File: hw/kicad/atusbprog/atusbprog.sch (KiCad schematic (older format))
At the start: 26 parts, among them J1 SMH-110-02-L-D, J2 Conn_01x04, J3 Conn_01x08, J4 Conn_01x08, J5 Conn_01x08, SW1 SW_Push, SW2 SW_Push, U1 SN74HCT125, U2 AT89S52-24PU, Y1 24 MHz

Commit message: Update to KiCAD 5.1.5, add silk marks
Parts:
- RN1: footprint Resistor_THT:R_Array_SIP9 -> Resistors_THT:R_Array_SIP9
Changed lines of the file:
@@
 EESchema Schematic File Version 4
-LIBS:atusbprog-cache
-EELAYER 26 0
+EELAYER 30 0
 EELAYER END
 $Descr A4 11693 8268
@@
 F 0 "RN1" H 10180 2196 50  0000 L CNN
 F 1 "1.2k" H 10180 2105 50  0000 L CNN
-F 2 "Resistor_THT:R_Array_SIP9" V 10275 2150 50  0001 C CNN
+F 2 "Resistors_THT:R_Array_SIP9" V 10275 2150 50  0001 C CNN
 F 3 "https://www.bourns.com/docs/Product-Datasheets/4600x.pdf" H 9800 2150 50  0001 C CNN
 	1    9800 2150

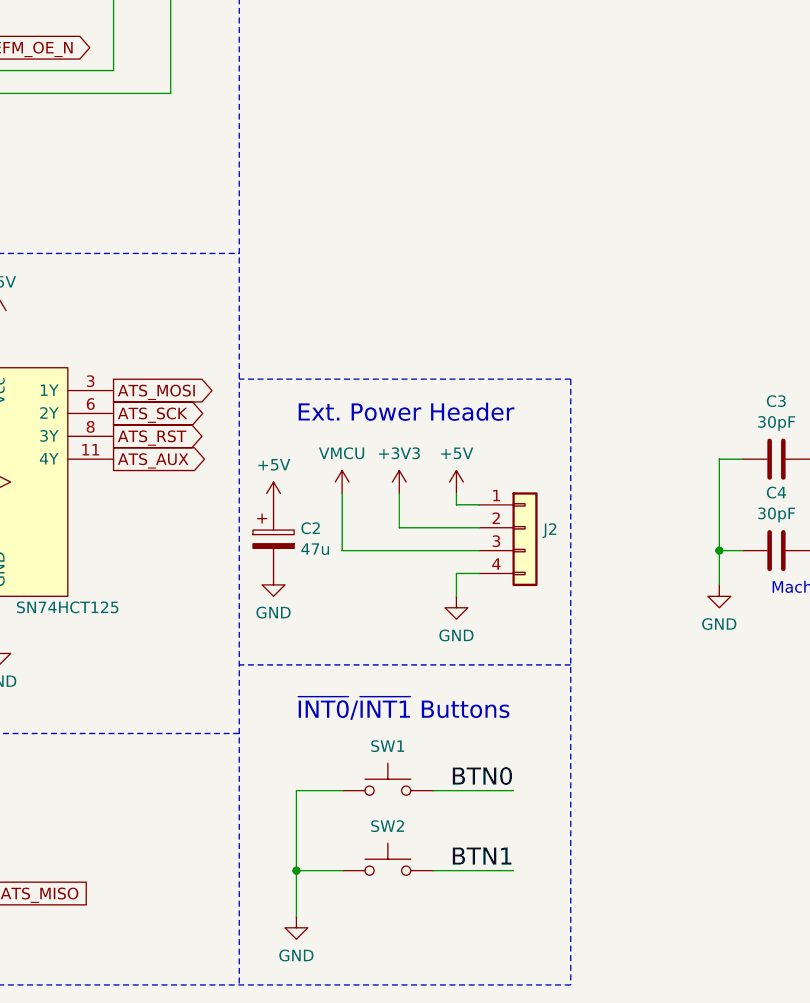
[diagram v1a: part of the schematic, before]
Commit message: Add power LEDs
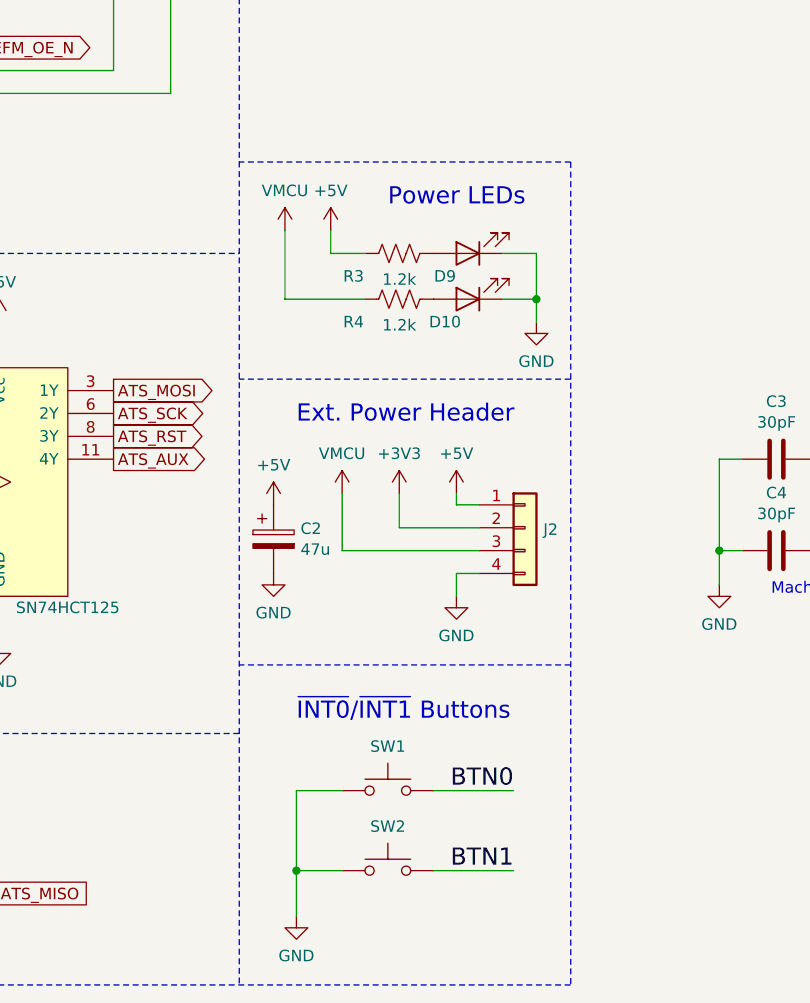
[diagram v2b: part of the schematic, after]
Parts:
- added D10: LTL2R3KYD-EM, LEDs:LED_D5.0mm, symbol Device:LED
- added D9: LTL2R3KRD-EM, LEDs:LED_D5.0mm, symbol Device:LED
- added R3, R4: 1.2k, Resistors_THT:R_Axial_DIN0207_L6.3mm_D2.5mm_P7.62mm_Horizontal, symbol Device:R_US
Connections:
- net +5V: now also R3.1
- net +VMCU: now also R4.1
- net GND: now also D10.1 (K), D9.1 (K)
- new net: D10.2 (A), R4.2
- new net: D9.2 (A), R3.2
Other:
- note added: "Power LEDs"
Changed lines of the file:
@@
 Ext. Power Header
-Wire Notes Line
-	4800 4350 4800 7000
 Wire Notes Line
 	4800 5600 3350 5600
 Wire Notes Line
 	4800 4350 3350 4350
+$Comp
+L Device:LED D10
+U 1 1 5E8A95B0
+P 4350 4000
+F 0 "D10" H 4450 4100 50  0000 C CNN
+F 1 "LTL2R3KYD-EM" V 4297 3883 50  0001 R CNN
+F 2 "LEDs:LED_D5.0mm" H 4350 4000 50  0001 C CNN
+F 3 "https://media.digikey.com/pdf/Data%20Sheets/Lite-On%20PDFs/LTL2R3KGD-EM%20Preliminary.pdf" H 4350 4000 50  0001 C CNN
+	1    4350 4000
+	-1   0    0    1
+$EndComp
+$Comp
+L Device:R_US R4
+U 1 1 5E8AEB1D
+P 4050 4000
+F 0 "R4" V 3950 4200 50  0000 C CNN
+F 1 "1.2k" V 3936 4000 50  0000 C CNN
+F 2 "Resistors_THT:R_Axial_DIN0207_L6.3mm_D2.5mm_P7.62mm_Horizontal" V 4090 3990 50  0001 C CNN
+F 3 "~" H 4050 4000 50  0001 C CNN
+	1    4050 4000
+	0    -1   -1   0
+$EndComp
+$Comp
+L power:GND #PWR03
+U 1 1 5E8E2789
+P 4650 4100
+F 0 "#PWR03" H 4650 3850 50  0001 C CNN
+F 1 "GND" H 4650 3927 50  0000 C CNN
+F 2 "" H 4650 4100 50  0001 C CNN
+F 3 "" H 4650 4100 50  0001 C CNN
+	1    4650 4100
+	1    0    0    -1
+$EndComp
+Wire Wire Line
+	4500 4000 4650 4000
+Wire Wire Line
+	4650 4000 4650 4100
+Wire Wire Line
+	4500 3800 4650 3800
+Wire Wire Line
+	4650 3800 4650 4000
+Connection ~ 4650 4000
+$Comp
+L Device:LED D9
+U 1 1 5E90859E
+P 4350 3800
+F 0 "D9" H 4450 3900 50  0000 C CNN
+F 1 "LTL2R3KRD-EM" V 4297 3683 50  0001 R CNN
+F 2 "LEDs:LED_D5.0mm" H 4350 3800 50  0001 C CNN
+F 3 "https://media.digikey.com/pdf/Data%20Sheets/Lite-On%20PDFs/LTL2R3KGD-EM%20Preliminary.pdf" H 4350 3800 50  0001 C CNN
+	1    4350 3800
+	-1   0    0    1
+$EndComp
+$Comp
+L Device:R_US R3
+U 1 1 5E908B0B
+P 4050 3800
+F 0 "R3" V 3950 4000 50  0000 C CNN
+F 1 "1.2k" V 3936 3800 50  0000 C CNN
+F 2 "Resistors_THT:R_Axial_DIN0207_L6.3mm_D2.5mm_P7.62mm_Horizontal" V 4090 3790 50  0001 C CNN
+F 3 "~" H 4050 3800 50  0001 C CNN
+	1    4050 3800
+	0    -1   -1   0
+$EndComp
+$Comp
+L atusbprog:+5V #PWR02
+U 1 1 5E909998
+P 3750 3700
+F 0 "#PWR02" H 3750 3550 50  0001 C CNN
+F 1 "+5V" H 3750 3874 50  0000 C CNN
+F 2 "" H 3750 3700 50  0001 C CNN
+F 3 "" H 3750 3700 50  0001 C CNN
+	1    3750 3700
+	1    0    0    -1
+$EndComp
+Wire Wire Line
+	3750 3700 3750 3800
+Wire Wire Line
+	3750 3800 3900 3800
+$Comp
+L atusbprog:VMCU #PWR01
+U 1 1 5E910D5D
+P 3550 3700
+F 0 "#PWR01" H 3550 3550 50  0001 C CNN
+F 1 "VMCU" H 3550 3874 50  0000 C CNN
+F 2 "" H 3550 3700 50  0001 C CNN
+F 3 "" H 3550 3700 50  0001 C CNN
+	1    3550 3700
+	1    0    0    -1
+$EndComp
+Wire Wire Line
+	3550 3700 3550 4000
+Wire Wire Line
+	3550 4000 3900 4000
+Text Notes 4000 3600 0    75   ~ 0
+Power LEDs
+Wire Notes Line
+	4800 3400 3350 3400
+Wire Notes Line
+	4800 3400 4800 7000
 $EndSCHEMATC
